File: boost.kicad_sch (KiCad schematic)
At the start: 24 parts, among them Q3 BSC059N04LS6, Q4 BSC059N04LS6, U7 LTC7804

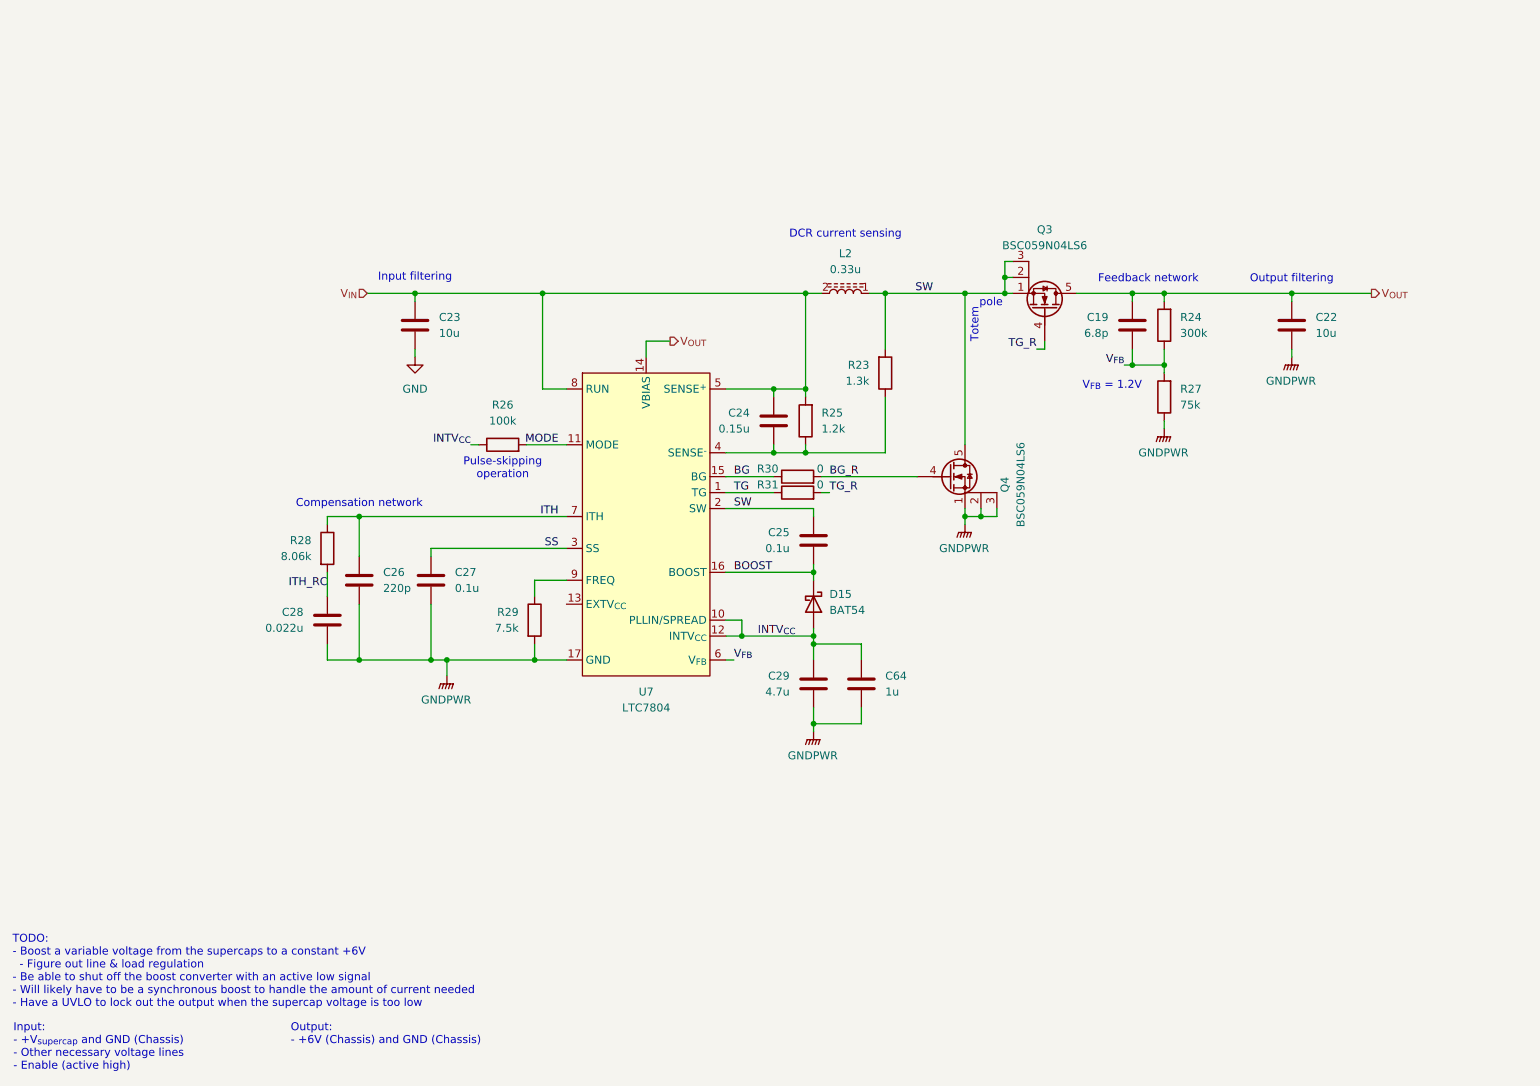
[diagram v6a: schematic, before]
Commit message: Changed output boost to be based on the LM5123-Q1
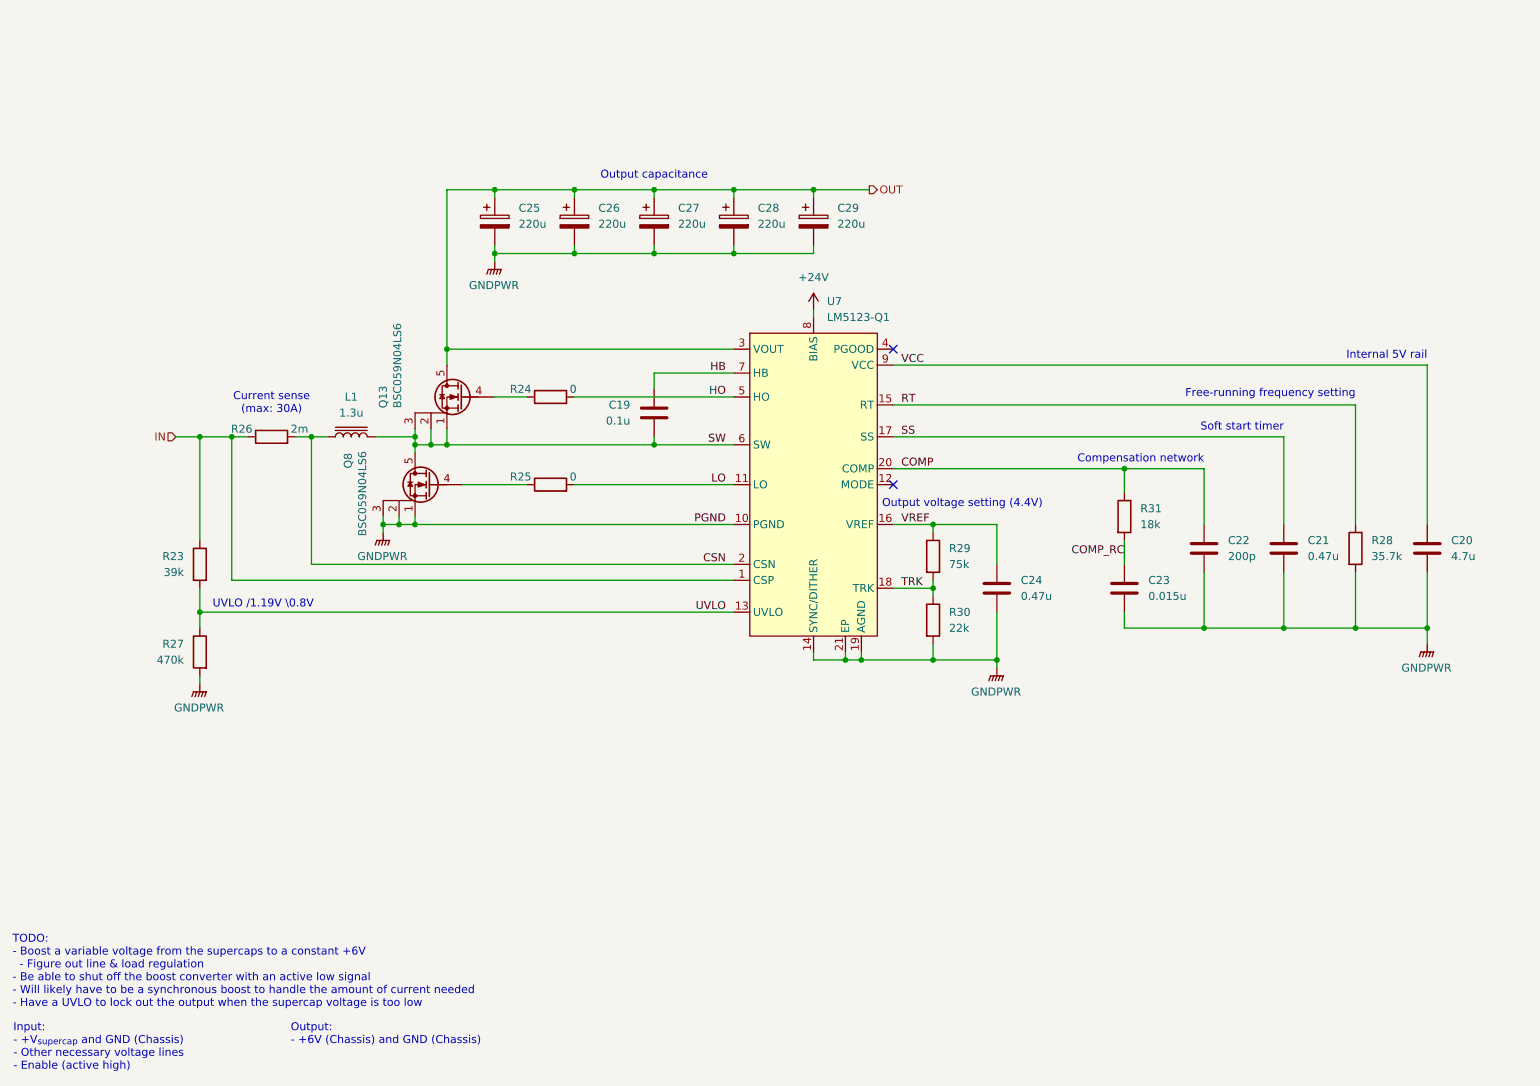
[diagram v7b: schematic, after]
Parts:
- removed C25, C27: 0.1u, Capacitor_SMD:C_0603_1608Metric_Pad1.08x0.95mm_HandSolder, symbol Device:C
- removed C26: 220p, Capacitor_SMD:C_0603_1608Metric_Pad1.08x0.95mm_HandSolder, symbol Device:C
- removed C28: 0.022u, Capacitor_SMD:C_0603_1608Metric_Pad1.08x0.95mm_HandSolder, symbol Device:C
- removed C29: 4.7u, Capacitor_SMD:C_0603_1608Metric_Pad1.08x0.95mm_HandSolder, symbol Device:C
- removed C64: 1u, Capacitor_SMD:C_0603_1608Metric_Pad1.08x0.95mm_HandSolder, symbol Device:C
- removed D15: BAT54, Package_TO_SOT_SMD:SOT-23_Handsoldering, symbol Device:D_Schottky
- removed L2: 0.33u, Inductor_SMD:L_Bourns_SRP7028A_7.3x6.6mm, symbol Device:L_Ferrite
- removed Q3, Q4: BSC059N04LS6, Package_SON:Infineon_PG-TDSON-8_6.15x5.15mm, symbol Transistor_FET:Q_NMOS_SGD
- removed U7: LTC7804, Package_DFN_QFN:QFN-16-1EP_3x3mm_P0.5mm_EP1.45x1.45mm, symbol ! Robomaster ICs:LTC7804
- added C20: 4.7u, Capacitor_SMD:C_0603_1608Metric_Pad1.08x0.95mm_HandSolder, symbol Device:C
- added C21: 0.47u, Capacitor_SMD:C_0603_1608Metric_Pad1.08x0.95mm_HandSolder, symbol Device:C
- added C25, C26, C27, C28, C29: 220u, Capacitor_THT:CP_Radial_D6.3mm_P2.50mm, symbol Device:C_Polarized
- added L1: 1.3u, symbol Device:L_Iron
- added Q13, Q8: BSC059N04LS6, Package_SON:Infineon_PG-TDSON-8_6.15x5.15mm, symbol Transistor_FET:Q_NMOS_SGD
- added U7: LM5123-Q1, Package_DFN_QFN:Texas_RGP0020H_VQFN-20-1EP_4x4mm_P0.5mm_EP2.4x2.4mm, symbol ! Robomaster ICs:LM5123-Q1
- C19: value 6.8p -> 0.1u
- C22: value 10u -> 200p; footprint Capacitor_SMD:C_0805_2012Metric_Pad1.18x1.45mm_HandSolder -> Capacitor_SMD:C_0603_1608Metric_Pad1.08x0.95mm_HandSolder; Mouser Part Number 187-CL21A106KAYNNNE -> (none)
- C23: value 10u -> 0.015u; footprint Capacitor_SMD:C_0805_2012Metric_Pad1.18x1.45mm_HandSolder -> Capacitor_SMD:C_0603_1608Metric_Pad1.08x0.95mm_HandSolder; Mouser Part Number 187-CL21A106KAYNNNE -> (none)
- C24: value 0.15u -> 0.47u
- R23: value 1.3k -> 39k
- R24: value 300k -> 0
- R25: value 1.2k -> 0; Mouser Part Number 603-RT0603FRE133K6L -> (none)
- R26: value 100k -> 2m
- R27: value 75k -> 470k
- R28: value 8.06k -> 35.7k
- R29: value 7.5k -> 75k
- R30: value 0 -> 22k
- R31: value 0 -> 18k
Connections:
- net BG_R is gone; now on net GNDPWR: R30.2
- net GND is gone; now on net GNDPWR: C23.2
- net ITH_RC is gone; now on net GNDPWR: R28.2
- net GNDPWR: now also C24.2, R27.2, C20.2, C21.2, C25.2, C26.2, C27.2, C28.2, C29.2, Q8.1 (S), Q8.2 (S), Q8.3 (S), U7.10 (PGND), U7.14 (SYNC/DITHER), U7.19 (AGND), U7.21 (EP); no longer R27.1, R29.2
- net SS: now also C21.1, U7.17 (SS)
- net SW: now also C19.2, L1.2, Q13.1 (S), Q13.2 (S), Q13.3 (S), Q8.5 (D), U7.6 (SW); no longer R23.2
- net VREF: now reaches R29.1
- net VREF: now also C24.1, U7.16 (VREF)
- net BG renamed TRK
- net TRK: now also R29.2, U7.18 (TRK)
- net INTV_{CC} renamed IN
- net IN: now also R23.1, U7.1 (CSP)
- net ITH renamed RT
- net RT: now also U7.15 (RT)
- net MODE renamed CSN
- net CSN: now also L1.1, U7.2 (CSN)
- net TG renamed COMP
- net COMP: now also C22.1, U7.20 (COMP)
- net TG_R renamed COMP_RC
- net COMP_RC: now also C23.1
- removed net V_{FB}: C19.2, R24.1, R27.2
- removed net V_{IN}: C23.1, C24.1, R25.2
- removed net V_{OUT}: C19.1, C22.1, R24.2
- new net: Q13.4 (G), R24.1
- new net: Q8.4 (G), R25.1
- new net +24V: U7.8 (BIAS)
- new net HB: C19.1, U7.7 (HB)
- new net HO: R24.2, U7.5 (HO)
- new net LO: R25.2, U7.11 (LO)
- new net OUT: C25.1, C26.1, C27.1, C28.1, C29.1, Q13.5 (D), U7.3 (VOUT)
- new net UVLO: R23.2, R27.1, U7.13 (UVLO)
- new net VCC: C20.1, U7.9 (VCC)
- no-connect marks 0 -> 2
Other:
- note added: "Current sense (max: 30A)"
- note added: "Free-running frequency setting"
- note added: "Internal 5V rail"
- note added: "Output capacitance"
- note added: "Output voltage setting (4.4V)"
- note added: "Soft start timer"
- note added: "UVLO /1.19V \0.8V"
- note removed: "DCR current sensing"
- note removed: "Feedback network"
- note removed: "Input filtering"
- note removed: "Output filtering"
- note removed: "Pulse-skipping operation"
- note removed: "Totem"
- note removed: "V_{FB} = 1.2V"
- note removed: "pole"
